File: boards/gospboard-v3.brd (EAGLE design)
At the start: 88.9 x 50.8 mm, 6 parts, among them IC1 MCP604P, IC2 MCP604P, J3 455-1750-1-ND

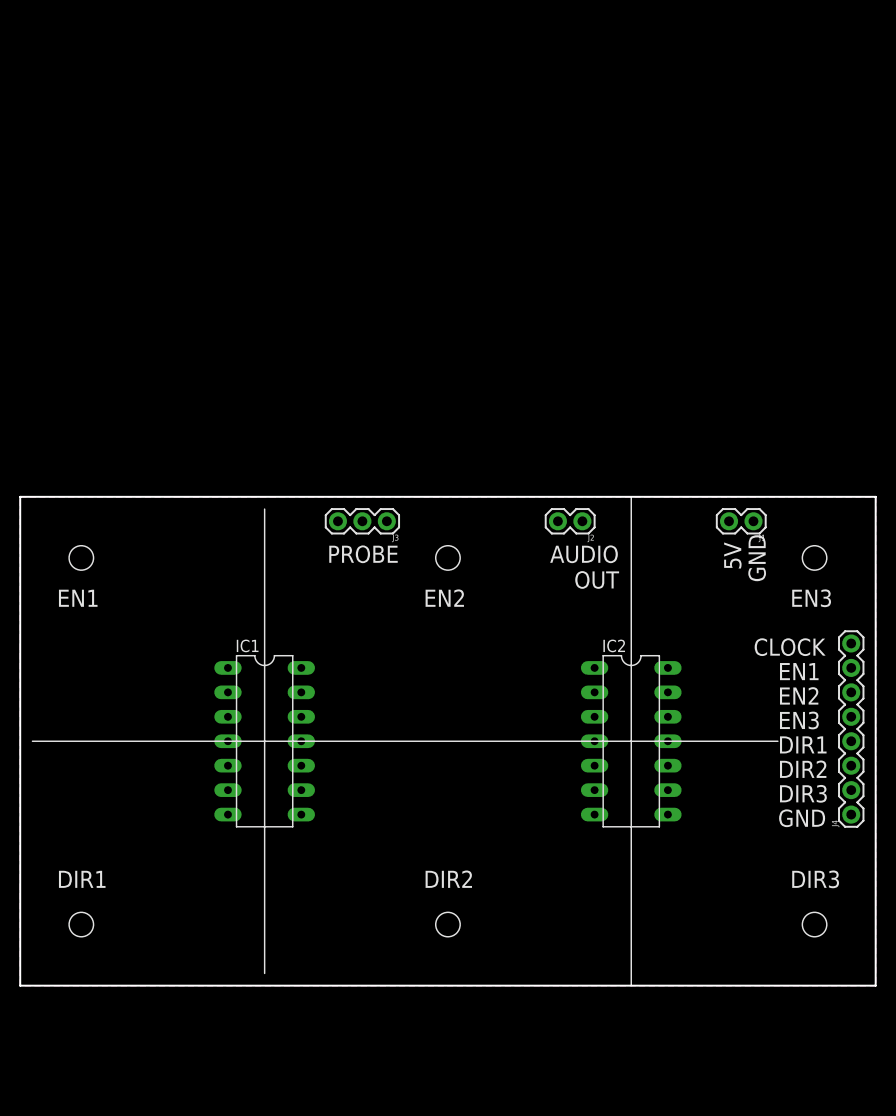
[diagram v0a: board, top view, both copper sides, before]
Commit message: trashotron board geometry roughed out with correct dimensions
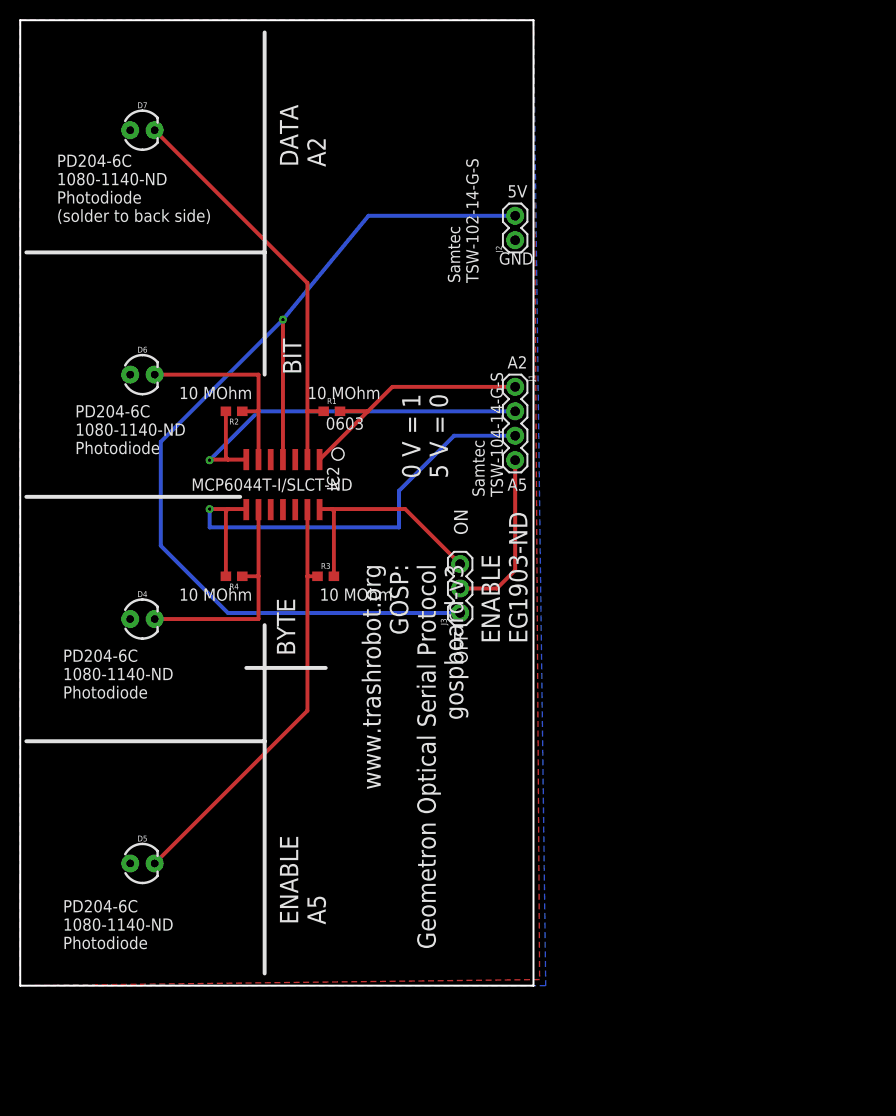
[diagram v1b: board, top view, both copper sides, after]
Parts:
- removed IC1: MCP604P, linear:DIL14
- removed J4: (no value), SparkFun-Connectors:1X08
- added D4, D5, D6, D7: (no value), SparkFun-LED:LED_3MM
- added R1, R2, R3, R4: 10M, SparkFun-Resistors:0603
- IC2: value MCP604P -> MCP604SL; device linear:DIL14 -> linear:SO14
- J1: device SparkFun-Connectors:1X02 -> SparkFun-Connectors:1X04
- moved IC2 45.0 mm to (27.3, 52.1), turned to 180 degrees
- moved J2 30.0 mm to (51.4, 77.5), turned to 90 degrees
- moved J1 28.4 mm to (51.4, 62.2), turned to 270 degrees
- moved J3 12.2 mm to (45.7, 38.7), turned to 90 degrees
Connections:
- removed net V+: IC1.4, IC2.4
- removed net V-: IC1.11, IC2.11
- new net ENABLE: IC2.14, J3.3, R3.2
- new net GND: D4.A, D5.A, D6.A, D7.A, IC2.10, IC2.11, IC2.12, IC2.3, IC2.5, J2.1
- new net N$10: D4.K, IC2.9, R4.1
- new net N$11: IC2.7, J1.2, R2.2
- new net N$13: D5.K, IC2.13, R3.1
- new net N$14: IC2.4, J2.2, J3.1
- new net N$5: J1.4, J3.2
- new net N$6: D7.K, IC2.2, R1.1
- new net N$8: IC2.8, J1.3, R4.2
- new net N$9: D6.K, IC2.6, R2.1
- new net PIN1: IC2.1, J1.1, R1.2
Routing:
- net N$14: track 0.00 -> 106.5 mm, vias 0 -> 1
- net N$8: track 0.00 -> 50.7 mm, vias 0 -> 1
- net N$13: track 0.00 -> 44.4 mm
- net N$11: track 0.00 -> 42.8 mm, vias 0 -> 1
- net N$6: track 0.00 -> 42.5 mm
- net PIN1: track 0.00 -> 26.4 mm
- net ENABLE: track 0.00 -> 24.1 mm
- net N$10: track 0.00 -> 23.9 mm
- net N$9: track 0.00 -> 21.3 mm
- net N$5: track 0.00 -> 17.9 mm
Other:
- board size 88.9 x 50.8 mm -> 53.3 x 100.3 mm
- board text added: "0 V = 1 5 V = 0"
- board text added: "0603"
- board text added: "10 MOhm"
- board text added: "A2"
- board text added: "A5"
- board text added: "BIT"
- board text added: "BYTE"
- board text added: "DATA A2"
- board text added: "ENABLE A5"
- board text added: "ENABLE EG1903-ND"
- board text added: "MCP6044T-I/SLCT-ND"
- board text added: "OFF"
- board text added: "ON"
- board text added: "PD204-6C 1080-1140-ND Photodiode"
- board text added: "PD204-6C 1080-1140-ND Photodiode (solder to back side)"
- board text added: "Samtec TSW-102-14-G-S"
- board text added: "Samtec TSW-104-14-G-S"
- board text added: "www.trashrobot.org"
- board text added: "www.trashrobot.org GOSP: Geometron Optical Serial Protocol gospboard-v3"
- board text removed: "AUDIO OUT"
- board text removed: "CLOCK"
- board text removed: "DIR1"
- board text removed: "DIR2"
- board text removed: "DIR3"
- board text removed: "EN1"
- board text removed: "EN2"
- board text removed: "EN3"
- board text removed: "PROBE"
